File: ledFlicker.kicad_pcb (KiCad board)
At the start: 2 copper layers, 30 x 44 mm, 48 parts, among them J1 Conn_01x04_Pin, J2 S2B-PH-K-SLFSN, J3 Conn_01x02_Pin, J4 USB_B_Micro, J5 Conn_01x02_Pin, Q1 BC817, U1 SPX3819M5-L, U2 MCP73831-2-OT, U4 TLC555xD, U5 TLC555xD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

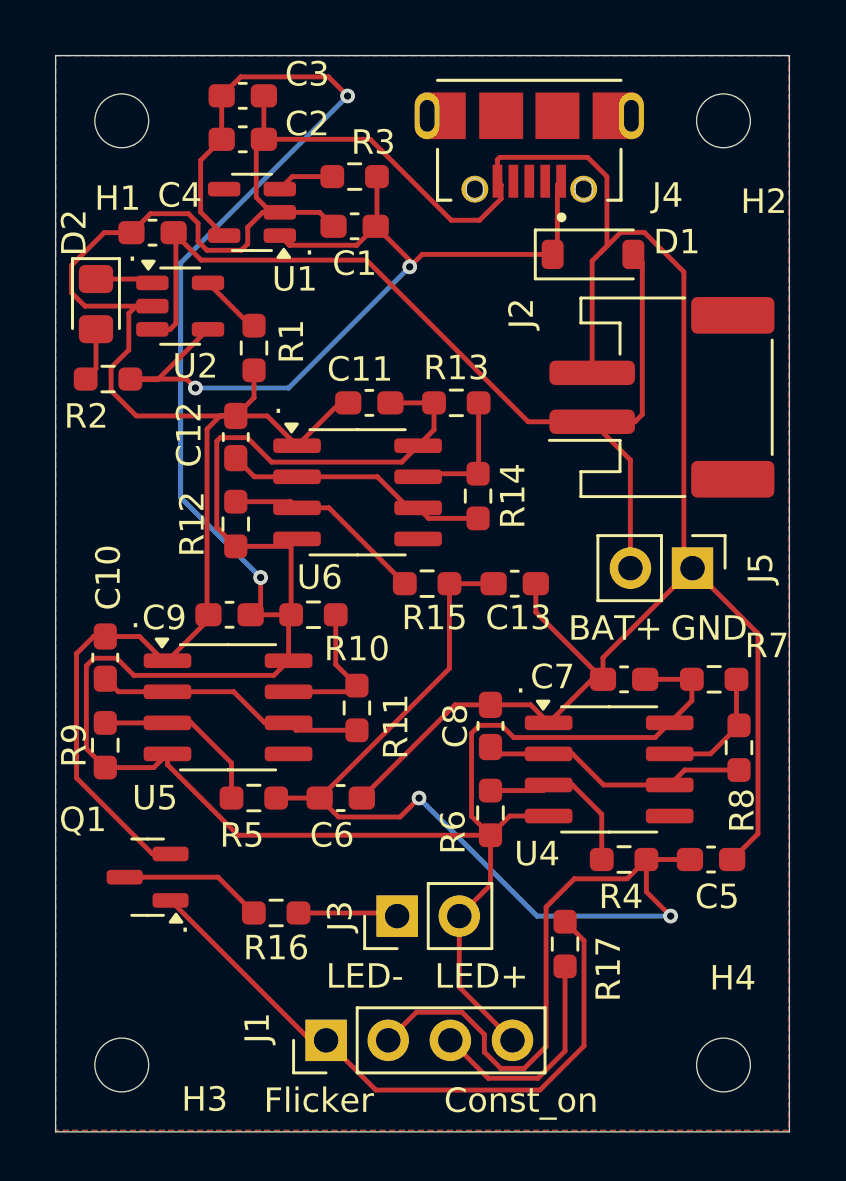
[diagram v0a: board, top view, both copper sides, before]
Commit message: Shrunk PCB size, updated switch to OFF, FLICKER only and added R17 bias resistor
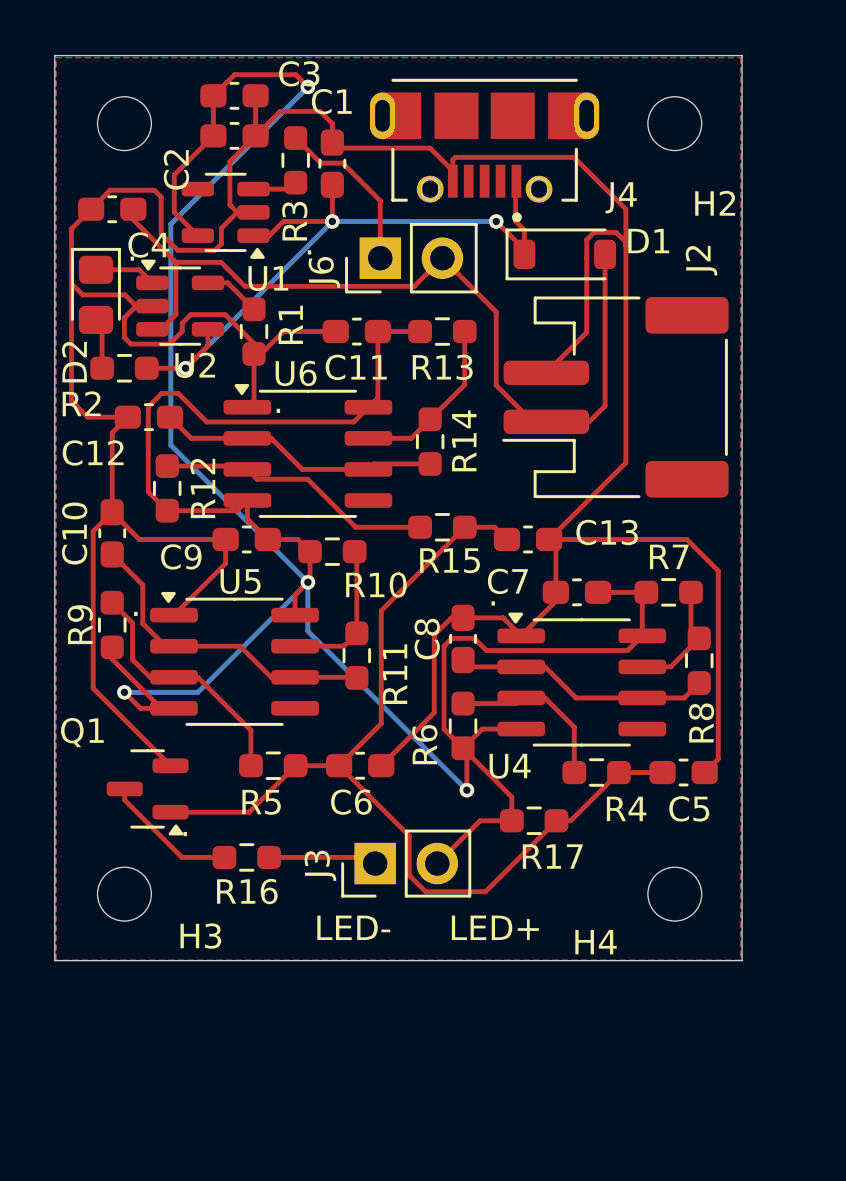
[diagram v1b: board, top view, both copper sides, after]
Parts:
- removed J1: Conn_01x04_Pin, Connector_PinHeader_2.54mm:PinHeader_1x04_P2.54mm_Vertical
- removed J5: Conn_01x02_Pin, Connector_PinHeader_2.54mm:PinHeader_1x02_P2.54mm_Vertical
- added J6: Conn_01x02_Pin, Connector_PinHeader_2.54mm:PinHeader_1x02_P2.54mm_Vertical, F.Cu at (160.0, 38.0)
- R17: value 1K -> 20K
- moved H4 7.26 mm to (172.0, 64.0)
- moved H3 6.99 mm to (149.5, 64.0)
- moved G*** 5.26 mm to (160.7, 46.5)
- moved R17 5.20 mm to (166.2, 61.0), turned to 0 degrees
- moved C10 5.09 mm to (149.0, 49.2)
- moved R9 4.92 mm to (149.0, 53.0)
- moved C7 4.04 mm to (168.0, 51.7)
- moved R7 4.01 mm to (171.8, 51.7)
- moved R8 3.91 mm to (173.0, 54.5)
- moved C5 3.73 mm to (172.4, 59.0)
- moved C8 3.73 mm to (163.3, 53.6)
- moved U4 3.73 mm to (168.2, 55.3)
- moved R6 3.73 mm to (163.3, 57.1)
- moved R4 3.73 mm to (168.8, 59.0)
- moved C12 3.64 mm to (150.5, 44.5), turned to 180 degrees
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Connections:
- C13 pad 1: Net-(J1-Pin_2) -> Net-(Q1-B)
- C5 pad 1: Net-(J1-Pin_2) -> Net-(Q1-B)
- C6 pad 1: Net-(J1-Pin_2) -> Net-(Q1-B)
- Q1 pad 1: Net-(J1-Pin_1) -> Net-(Q1-B)
- R15 pad 2: Net-(J1-Pin_2) -> Net-(Q1-B)
- R17 pad 1: Net-(J1-Pin_1) -> +3V3
- R17 pad 2: Net-(J1-Pin_3) -> Net-(Q1-B)
- R3 pad 1: VBUS -> Net-(U1-EN)
- R3 pad 2: Net-(U1-EN) -> /EN
- R4 pad 2: Net-(J1-Pin_2) -> Net-(Q1-B)
- R5 pad 2: Net-(J1-Pin_2) -> Net-(Q1-B)
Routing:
- net Net-(J1-Pin_2): track 55.3 -> 0.00 mm, vias 2 -> 0
- net Net-(Q1-B): track 0.00 -> 39.8 mm
- net Net-(J1-Pin_1): track 26.3 -> 0.00 mm
- net Net-(J1-Pin_3): track 9.25 -> 0.00 mm
- net /EN: track 0.00 -> 6.87 mm
- net VBUS: track 35.5 -> 28.7 mm, vias 2 -> 3
- net GND: track 149.8 -> 144.0 mm
- net VDC: track 40.6 -> 35.7 mm
- net +3V3: track 125.4 -> 121.5 mm, vias 2 -> 4
- net /Osc_3: track 8.30 -> 11.4 mm
- net /Osc_2: track 7.27 -> 10.2 mm
- net Net-(U5-THR): track 11.2 -> 13.0 mm
- net Net-(U6-DIS): track 5.41 -> 7.02 mm
- net Net-(U6-THR): track 10.9 -> 11.6 mm
- net Net-(U1-EN): track 2.36 -> 1.83 mm
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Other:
- board size 30 x 44 mm -> 28.1 x 37 mm
- board text removed: "BAT+"
- board text removed: "Const_on"
- board text removed: "Flicker"
- board text removed: "GND"
